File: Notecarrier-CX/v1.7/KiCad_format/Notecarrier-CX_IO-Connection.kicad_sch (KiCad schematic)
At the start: 12 parts, among them J1 BM04B-SRSS-TB(LF)(SN), P1 Header Castellated 2.54mm 1X16, P2 Header Castellated 2.54mm 1X16, P3 12402012E212A, P4 Header 2.54mm 1x5, P5 S2B-PH-SM4-K-TB, U1 NX3DV42GU

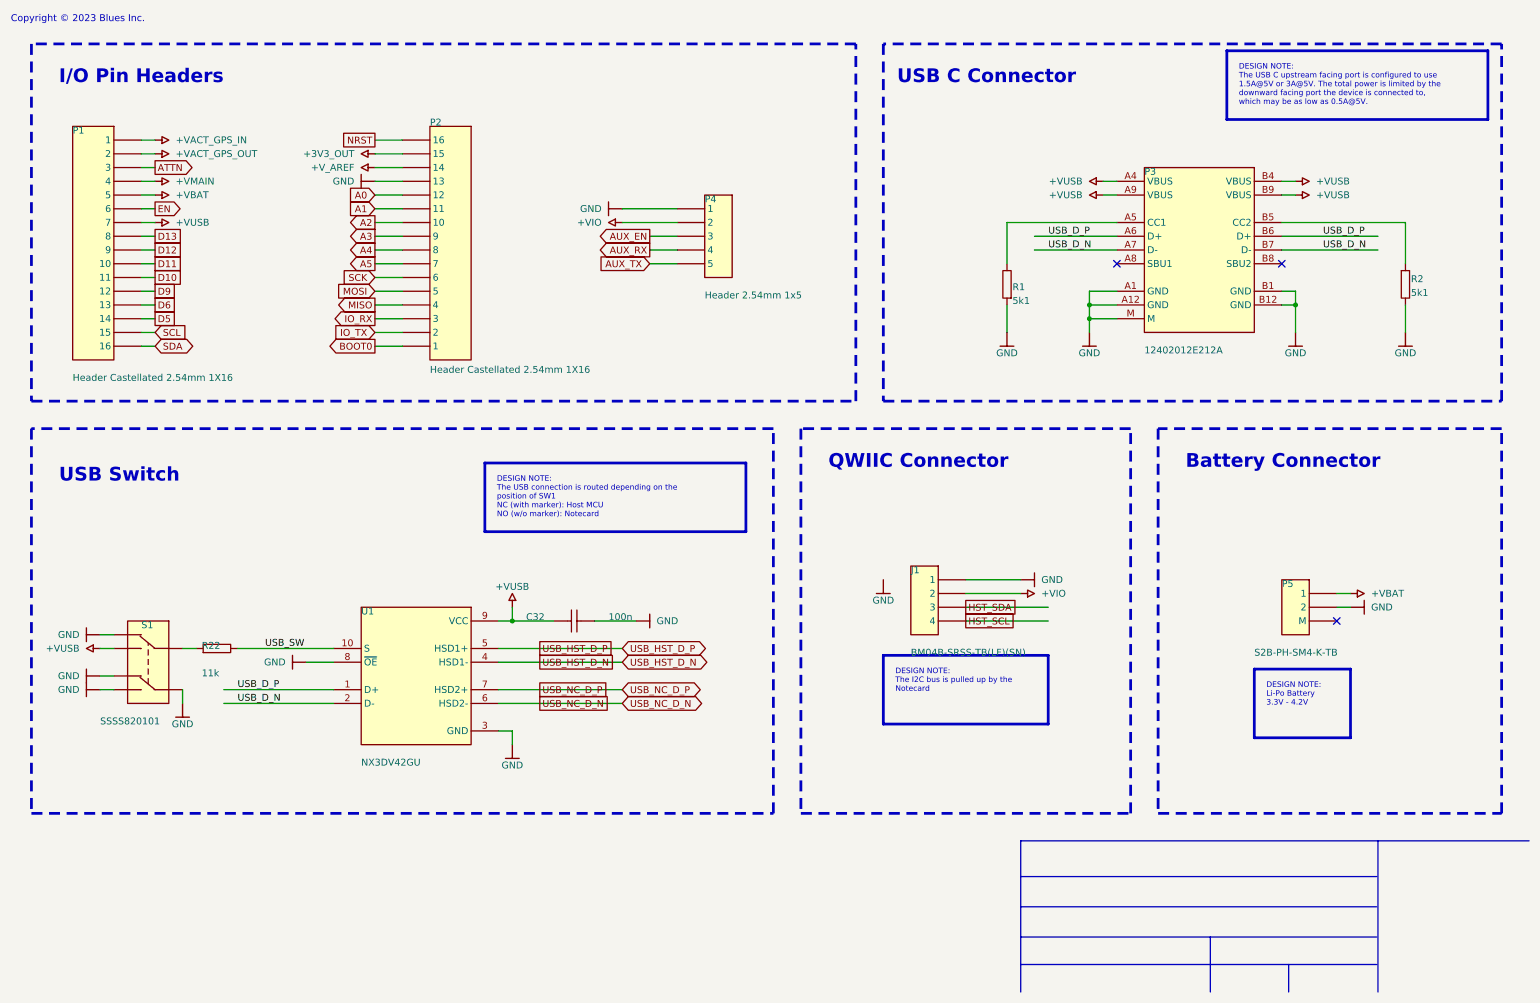
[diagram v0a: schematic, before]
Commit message: Ports: convert design-note text_boxes to plain text so kicanvas can render them
kicanvas parses text_box but never paints it - true of the current upstream
build too, which is byte-identical to the one vendored here. On the published
datasheet pages that left the design notes (charger limits, regulator specs,
population notes) as empty frames, and on Cygnet, whose note frames ARE the
text_boxes, the notes were entirely invisible. KiCad renders plain text and
rectangles identically to what it drew before, and kicanvas renders both, so
the 28 text_boxes across 12 sheets on 6 boards become plain text items - plus a
synthesized rectangle carrying the exact stroke and fill for the 5 Cygnet notes
whose box itself is visible (yellow-filled with a border).

Two things made this more than a mechanical swap:

- text_box soft-wraps and plain text does not. A first attempt left two notes
  overflowing their frames and colliding with a neighbouring note. The wrap is
  now frozen at exactly the line breaks KiCad itself used: each sheet's
  before-conversion PDF carries a hidden searchable text layer, and the
  converter reads the wrapped lines out of the note's own rectangle, guarded by
  a word-for-word equality check against the source text. That guard earned its
  keep twice, catching part-number labels that physically overlap two of the
  note boxes.

- kicanvas draws default-colored text in its theme color, which is white - and
  two Cygnet notes sit on yellow fills. Those five framed notes now carry an
  explicit (0,0,193) font color, sampled from KiCad's own plot of the same
  notes, so KiCad's output is unchanged and kicanvas is readable.

Verified per board: netlists byte-equal before and after; KiCad PDF renders
differ only by sub-millimetre line pitch (0.05-0.7% of sampled pixels, every
note inside its frame - checked visually on the worst sheets); kicanvas renders
all 12 sheets with the notes now visible; committed screenshots regenerated,
all six boards PASS.

Co-Aut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
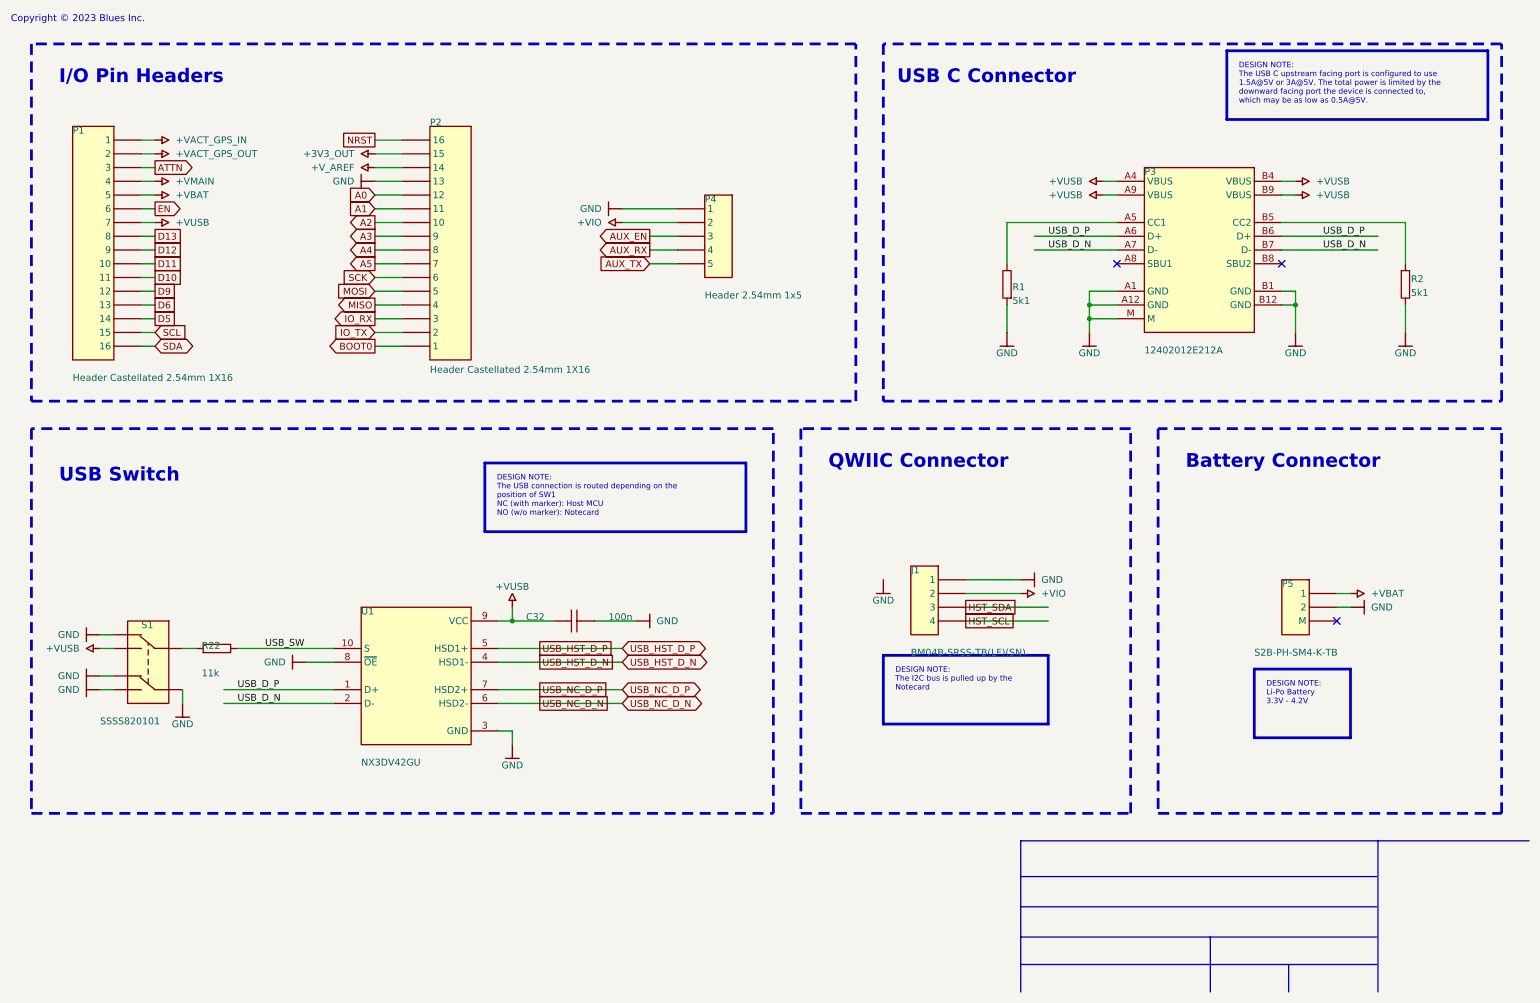
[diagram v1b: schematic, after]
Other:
- note added: "DESIGN NOTE: Li-Po Battery 3.3V - 4.2V"
- note added: "DESIGN NOTE: The I2C bus is pulled up by the Notecard"
- note added: "DESIGN NOTE: The USB C upstream facing port is configured to use 1.5A@5V or 3A@5V. The total power is limited by the downward facing port the device is connected to, which may be as low as 0.5A@5V."
- note added: "DESIGN NOTE: The USB connection is routed depending on the position of SW1 NC (with marker): Host MCU NO (w/o marker): Notecard"
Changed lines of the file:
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@@
 		)
 	)
-	(text_box "DESIGN NOTE:\nThe I2C bus is pulled up by the Notecard\n"
+	(text "DESIGN NOTE:\nThe I2C bus is pulled up by the\nNotecard\n"
 		(exclude_from_sim no)
-		(at 196.85 143.9672 0)
-		(size -27.94 10.16)
-		(margins 0.9525 0.9525 0.9525 0.9525)
-		(stroke
-			(width -0.0001)
-			(type default)
-			(color 0 0 0 1)
-		)
-		(fill
-			(type none)
-		)
+		(at 169.862 144.92 0)
 		(effects
 			(font
@@
 		)
 	)
-	(text_box "DESIGN NOTE:\nLi-Po Battery\n3.3V - 4.2V"
+	(text "DESIGN NOTE:\nLi-Po Battery\n3.3V - 4.2V"
 		(exclude_from_sim no)
-		(at 256.54 146.5072 0)
-		(size -19.05 10.16)
-		(margins 0.9525 0.9525 0.9525 0.9525)
-		(stroke
-			(width -0.0001)
-			(type default)
-			(color 0 0 0 1)
-		)
-		(fill
-			(type none)
-		)
+		(at 238.442 147.46 0)
 		(effects
 			(font
@@
 		)
 	)
-	(text_box "DESIGN NOTE:\nThe USB C upstream facing port is configured to use 1.5A@5V or 3A@5V. The total power is limited by the downward facing port the device is connected to, which may be as low as 0.5A@5V."
+	(text "DESIGN NOTE:\nThe USB C upstream facing port is configured to use\n1.5A@5V or 3A@5V. The total power is limited by the\ndownward facing port the device is connected to,\nwhich may be as low as 0.5A@5V."
 		(exclude_from_sim no)
-		(at 276.86 32.2072 0)
-		(size -44.45 10.16)
-		(margins 0.9525 0.9525 0.9525 0.9525)
-		(stroke
-			(width -0.0001)
-			(type default)
-			(color 0 0 0 1)
-		)
-		(fill
-			(type none)
-		)
+		(at 233.363 33.1597 0)
 		(effects
 			(font
@@
 		)
 	)
-	(text_box "DESIGN NOTE:\nThe USB connection is routed depending on the position of SW1\nNC (with marker): Host MCU\nNO (w/o marker): Notecard\n"
+	(text "DESIGN NOTE:\nThe USB connection is routed depending on the\nposition of SW1\nNC (with marker): Host MCU\nNO (w/o marker): Notecard\n"
 		(exclude_from_sim no)
-		(at 139.7 108.4072 0)
-		(size -44.45 10.16)
-		(margins 0.9525 0.9525 0.9525 0.9525)
-		(stroke
-			(width -0.0001)
-			(type default)
-			(color 0 0 0 1)
-		)
-		(fill
-			(type none)
-		)
+		(at 96.2025 109.36 0)
 		(effects
 			(font
